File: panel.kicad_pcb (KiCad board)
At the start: 2 copper layers, 74.4 x 74.4 mm, 92 parts, among them J1 JST_SH_SM06B-SRSS-TB_1x06-1MP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, J2 Input0, J3 Input1, J4 Conn_01x04, U1 M24C02-FMN

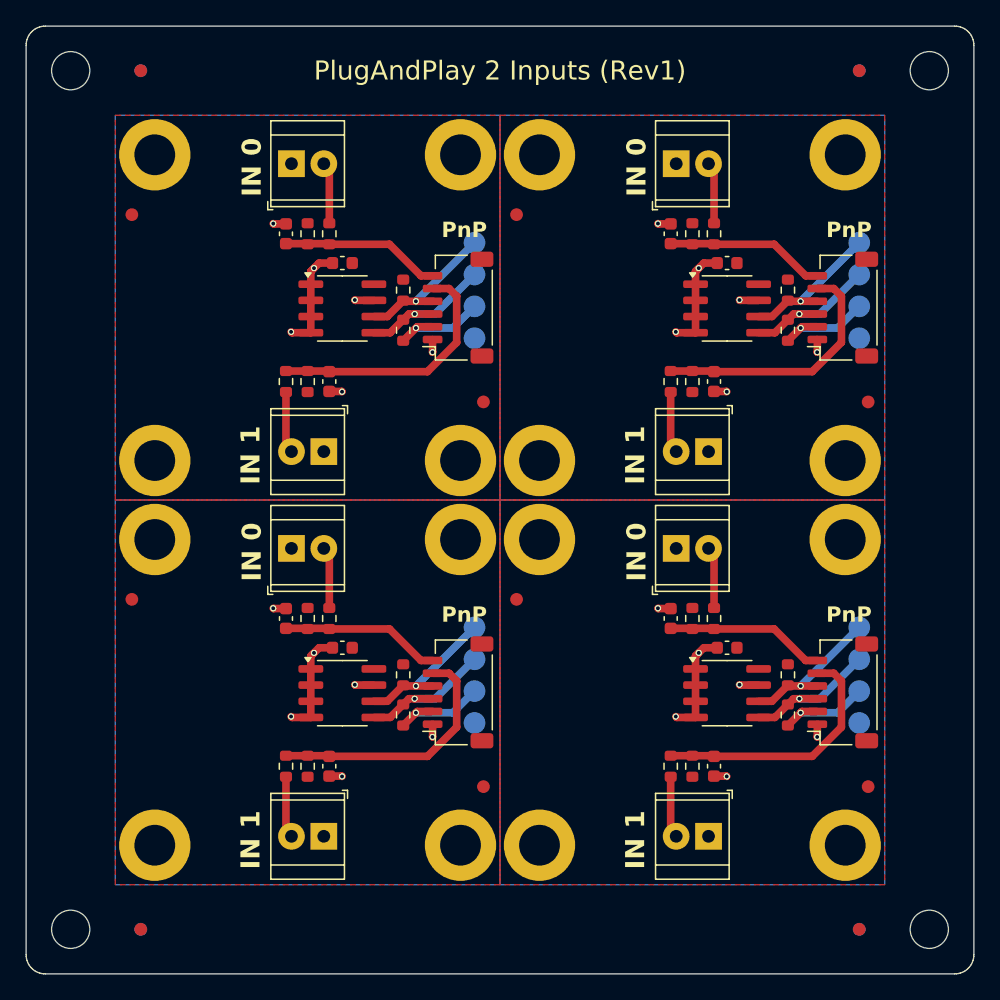
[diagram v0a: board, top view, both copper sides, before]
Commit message: Change screw terminals to 3.5mm version
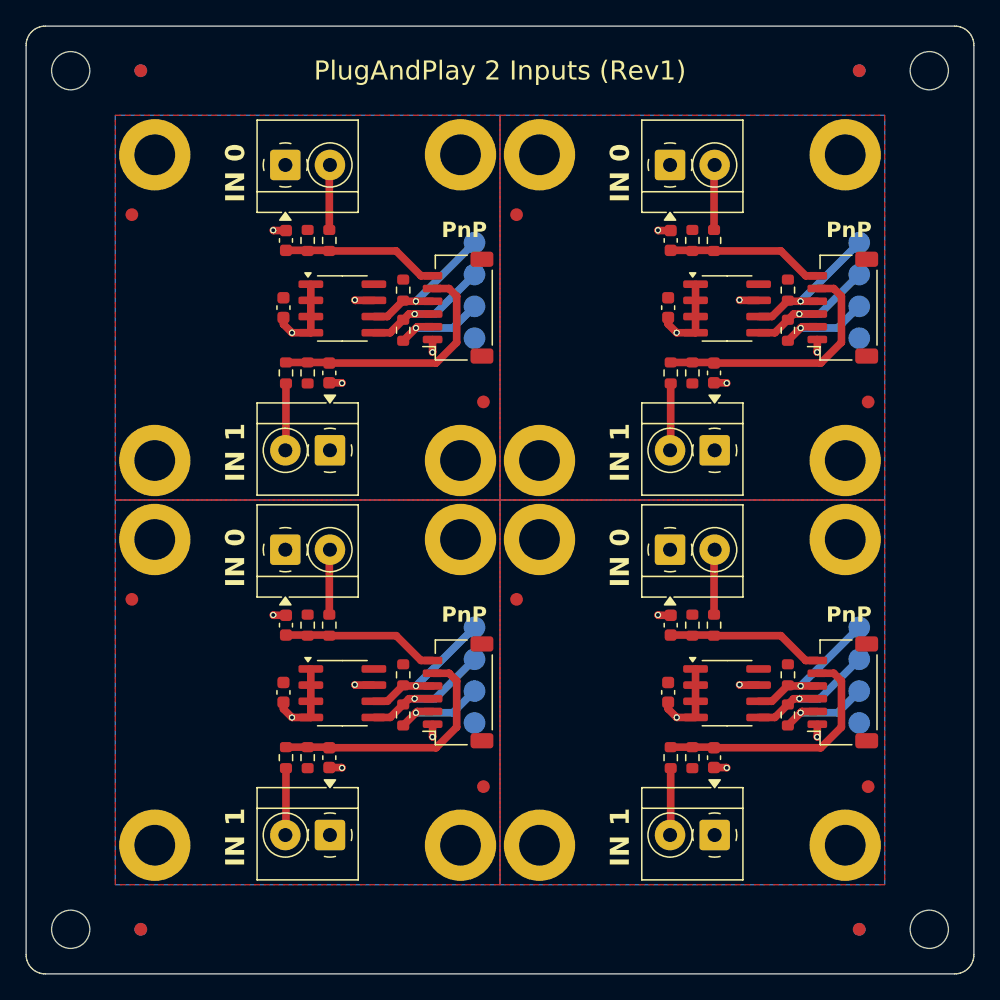
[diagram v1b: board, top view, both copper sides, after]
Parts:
- removed the C1 at (122.8, 68.8)
- removed the C1 at (122.8, 38.6)
- removed the C1 at (92.6, 68.8)
- removed the C1 at (92.6, 38.6)
- removed the C2 at (88.2, 66.5)
- removed the C2 at (118.4, 36.3)
- removed the C2 at (118.4, 66.5)
- removed the C2 at (88.2, 36.3)
- removed the C3 at (121.8, 78.1)
- removed the C3 at (91.6, 78.1)
- removed the C3 at (121.8, 47.9)
- removed the C3 at (91.6, 47.9)
- removed the J2 at (91.2, 83.6)
- removed the J2 at (121.4, 53.4)
- removed the J2 at (121.4, 83.6)
- removed the J2 at (91.2, 53.4)
- removed the J3 at (88.6, 61.0)
- removed the J3 at (88.6, 30.8)
- removed the J3 at (118.8, 30.8)
- removed the J3 at (118.8, 61.0)
- removed the R1 at (120.1, 36.3)
- removed the R1 at (120.1, 66.5)
- removed the R1 at (89.9, 36.3)
- removed the R1 at (89.9, 66.5)
- removed the R2 at (121.8, 66.5)
- removed the R2 at (91.6, 36.3)
- removed the R2 at (91.6, 66.5)
- removed the R2 at (121.8, 36.3)
- removed the R3 at (88.2, 47.9)
- removed the R3 at (88.2, 78.1)
- removed the R3 at (118.4, 47.9)
- removed the R3 at (118.4, 78.1)
- removed the R4 at (89.9, 47.9)
- removed the R4 at (120.1, 78.1)
- removed the R4 at (89.9, 78.1)
- removed the R4 at (120.1, 47.9)
- added C1: 0.1uF, Capacitor_SMD:C_0603_1608Metric, F.Cu at (118.2, 72.3)
- added C1: 0.1uF, Capacitor_SMD:C_0603_1608Metric, F.Cu at (118.2, 42.1)
- added C1: 0.1uF, Capacitor_SMD:C_0603_1608Metric, F.Cu at (88.0, 42.1)
- added C1: 0.1uF, Capacitor_SMD:C_0603_1608Metric, F.Cu at (88.0, 72.3)
- added C2: 0.1uF, Capacitor_SMD:C_0603_1608Metric, F.Cu at (88.2, 36.8)
- added C2: 0.1uF, Capacitor_SMD:C_0603_1608Metric, F.Cu at (118.4, 67.0)
- added C2: 0.1uF, Capacitor_SMD:C_0603_1608Metric, F.Cu at (88.2, 67.0)
- added C2: 0.1uF, Capacitor_SMD:C_0603_1608Metric, F.Cu at (118.4, 36.8)
- added C3: 0.1uF, Capacitor_SMD:C_0603_1608Metric, F.Cu at (121.8, 47.2)
- added C3: 0.1uF, Capacitor_SMD:C_0603_1608Metric, F.Cu at (91.6, 77.4)
- added C3: 0.1uF, Capacitor_SMD:C_0603_1608Metric, F.Cu at (121.8, 77.4)
- added C3: 0.1uF, Capacitor_SMD:C_0603_1608Metric, F.Cu at (91.6, 47.2)
- added J2: Input0, TerminalBlock_4Ucon:TerminalBlock_4Ucon_1x02_P3.50mm_Horizontal, F.Cu at (91.7, 83.5)
- added J2: Input0, TerminalBlock_4Ucon:TerminalBlock_4Ucon_1x02_P3.50mm_Horizontal, F.Cu at (121.8, 83.5)
- added J2: Input0, TerminalBlock_4Ucon:TerminalBlock_4Ucon_1x02_P3.50mm_Horizontal, F.Cu at (121.8, 53.3)
- added J2: Input0, TerminalBlock_4Ucon:TerminalBlock_4Ucon_1x02_P3.50mm_Horizontal, F.Cu at (91.7, 53.3)
- added J3: Input1, TerminalBlock_4Ucon:TerminalBlock_4Ucon_1x02_P3.50mm_Horizontal, F.Cu at (118.3, 30.9)
- added J3: Input1, TerminalBlock_4Ucon:TerminalBlock_4Ucon_1x02_P3.50mm_Horizontal, F.Cu at (88.2, 30.9)
- added J3: Input1, TerminalBlock_4Ucon:TerminalBlock_4Ucon_1x02_P3.50mm_Horizontal, F.Cu at (118.3, 61.1)
- added J3: Input1, TerminalBlock_4Ucon:TerminalBlock_4Ucon_1x02_P3.50mm_Horizontal, F.Cu at (88.2, 61.1)
- added R1: 10K, Resistor_SMD:R_0603_1608Metric, F.Cu at (89.9, 36.8)
- added R1: 10K, Resistor_SMD:R_0603_1608Metric, F.Cu at (120.1, 36.8)
- added R1: 10K, Resistor_SMD:R_0603_1608Metric, F.Cu at (120.1, 67.0)
- added R1: 10K, Resistor_SMD:R_0603_1608Metric, F.Cu at (89.9, 67.0)
- added R2: 1K, Resistor_SMD:R_0603_1608Metric, F.Cu at (121.8, 67.0)
- added R2: 1K, Resistor_SMD:R_0603_1608Metric, F.Cu at (91.6, 67.0)
- added R2: 1K, Resistor_SMD:R_0603_1608Metric, F.Cu at (121.8, 36.8)
- added R2: 1K, Resistor_SMD:R_0603_1608Metric, F.Cu at (91.6, 36.8)
- added R3: 1K, Resistor_SMD:R_0603_1608Metric, F.Cu at (118.4, 47.2)
- added R3: 1K, Resistor_SMD:R_0603_1608Metric, F.Cu at (118.4, 77.4)
- added R3: 1K, Resistor_SMD:R_0603_1608Metric, F.Cu at (88.2, 77.4)
- added R3: 1K, Resistor_SMD:R_0603_1608Metric, F.Cu at (88.2, 47.2)
- added R4: 10K, Resistor_SMD:R_0603_1608Metric, F.Cu at (89.9, 77.4)
- added R4: 10K, Resistor_SMD:R_0603_1608Metric, F.Cu at (120.1, 47.2)
- added R4: 10K, Resistor_SMD:R_0603_1608Metric, F.Cu at (89.9, 47.2)
- added R4: 10K, Resistor_SMD:R_0603_1608Metric, F.Cu at (120.1, 77.4)
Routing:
- net Board_1-GND: track 13.3 -> 11.3 mm, vias 6 -> 5
- net Board_3-GND: track 13.3 -> 11.3 mm, vias 6 -> 5
- net Board_0-GND: track 13.3 -> 11.3 mm, vias 6 -> 5
- net Board_2-GND: track 13.3 -> 11.3 mm, vias 6 -> 5
- net Board_1-Net-(J2-Pin_2): track 4.85 -> 5.88 mm
- net Board_3-Net-(J2-Pin_2): track 4.85 -> 5.88 mm
- net Board_0-Net-(J2-Pin_2): track 4.85 -> 5.88 mm
- net Board_2-Net-(J2-Pin_2): track 4.85 -> 5.88 mm
- net Board_2-Net-(J3-Pin_2): track 4.85 -> 5.80 mm
- net Board_0-Net-(J3-Pin_2): track 4.85 -> 5.80 mm
- net Board_3-Net-(J3-Pin_2): track 4.85 -> 5.80 mm
- net Board_1-Net-(J3-Pin_2): track 4.85 -> 5.80 mm
